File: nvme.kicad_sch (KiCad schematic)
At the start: 7 parts, among them J3 pcie_m2_ngff, U19 ISL91127IRNZ

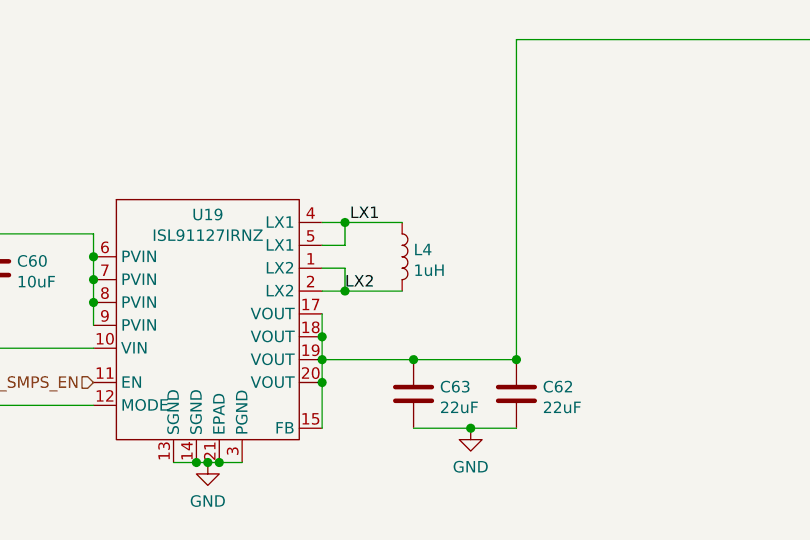
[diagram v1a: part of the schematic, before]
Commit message: Update to Kicad 6.0.0
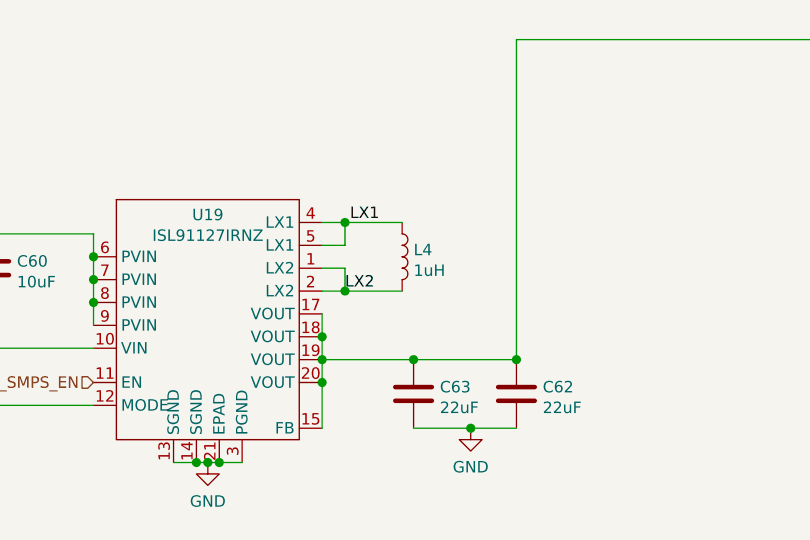
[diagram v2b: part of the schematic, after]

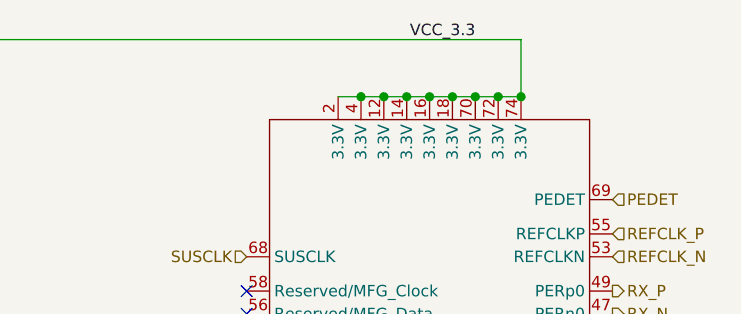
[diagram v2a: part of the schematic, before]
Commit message: Remove tlv320aic3206 and bq25895 and supporting circuitry from schematic; wire up audio/battery connections to Radxa CM3 third connector instead.
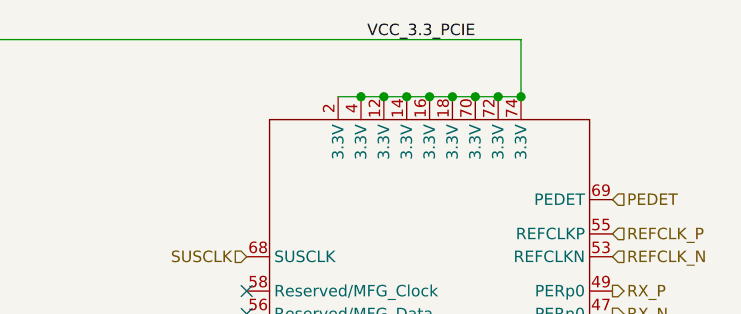
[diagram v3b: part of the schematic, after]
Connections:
- net VCC_3.3 renamed VCC_3.3_PCIE
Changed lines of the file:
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@@
     (stroke (width 0) (type solid) (color 0 0 0 0))
   )
-  (label "VCC_3.3" (at 223.52 50.8 180)
+  (label "VCC_3.3_PCIE" (at 223.52 50.8 180)
     (effects (font (size 1.27 1.27)) (justify right bottom))
   )
@@
       (effects (font (size 1.27 1.27)) hide)
     )
-    (property "Datasheet" "" (id 3) (at 92.71 82.55 0)
+    (property "Datasheet" "${KIPRJMOD}/datasheets/REN_isl91127ir_DST_20160301.pdf" (id 3) (at 92.71 82.55 0)
       (effects (font (size 1.27 1.27)) hide)
     )
